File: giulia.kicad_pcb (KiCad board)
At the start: 2 copper layers, 240.9 x 112.5 mm, 129 parts, among them J1 AVR-ISP-6, J2 0548190519, SW1 RESET, SW2 BOOT, U1 ATmega32A-PU, Y1 16 MHz

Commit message: rev1 of routing done
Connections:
- U1 pad 18: Net-(U1-Pad18) -> RGB
- U1 pad 20: RGB -> Net-(U1-Pad20)
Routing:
- net +5V: track 139.9 -> 772.8 mm, vias 1 -> 3
- net GND: track 155.9 -> 781.5 mm
- net SDA: track 0.00 -> 100.2 mm, vias 0 -> 1
- net SCL: track 0.00 -> 96.6 mm, vias 0 -> 1
- net Net-(D50-Pad4): track 0.00 -> 83.5 mm, vias 0 -> 1
- net Net-(D51-Pad2): track 0.00 -> 66.6 mm, vias 0 -> 2
- net Net-(D52-Pad2): track 0.00 -> 65.0 mm
- net Net-(D56-Pad2): track 0.00 -> 48.7 mm
- net Net-(D50-Pad2): track 0.00 -> 46.5 mm
- net Net-(D53-Pad2): track 0.00 -> 42.1 mm
- net Net-(D63-Pad2): track 0.00 -> 35.9 mm
- net Net-(D59-Pad2): track 0.00 -> 33.1 mm
- net Net-(D60-Pad2): track 0.00 -> 33.0 mm
- net Net-(D57-Pad2): track 0.00 -> 32.0 mm
- net Net-(D62-Pad2): track 0.00 -> 32.0 mm
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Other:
- board text added: "BOOT"
- board text added: "RESET"

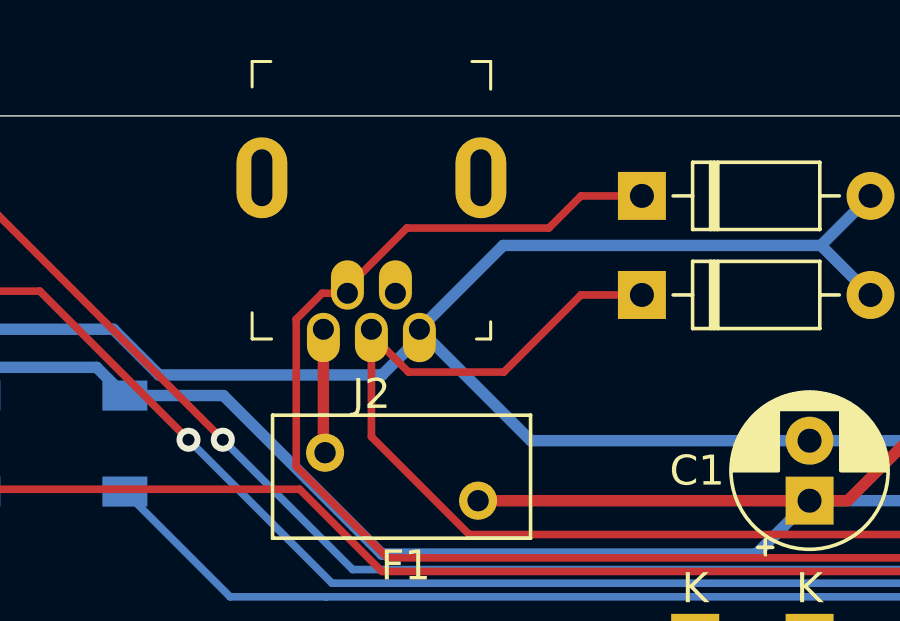
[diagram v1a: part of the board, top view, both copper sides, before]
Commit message: moved USB footprint to own lib
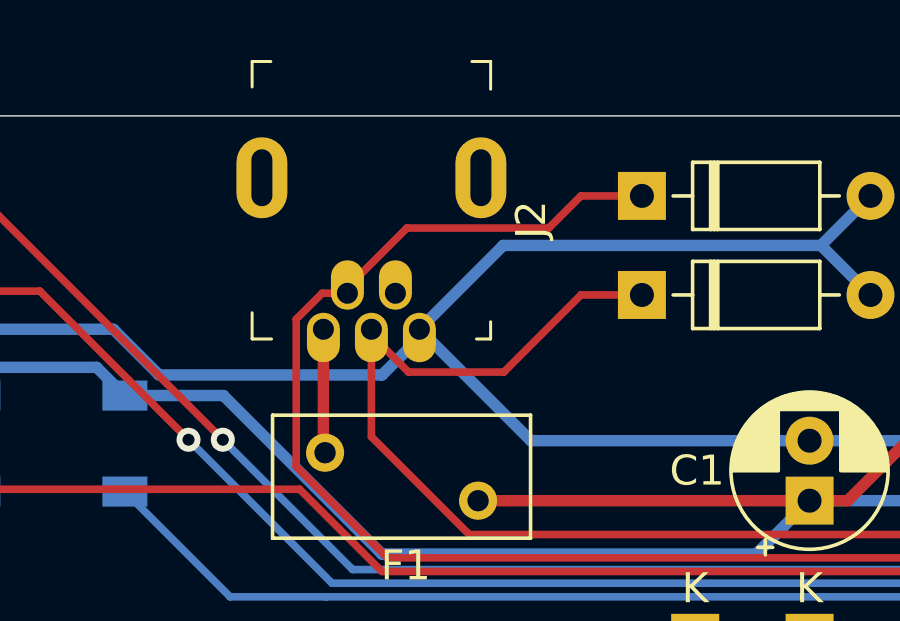
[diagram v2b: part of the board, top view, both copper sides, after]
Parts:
- J2: footprint digikey-footprints:USB_Mini_B_Female_548190519 -> giulia:USB_Mini_B_Female_548190519
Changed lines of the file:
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@@
     (add_net VCC)
   )
+  (module giulia:USB_Mini_B_Female_548190519 (layer F.Cu)
+    (at 94.615 27.686 270)
+    (fp_text reference J2 (at -3.65 -5.325 90) (layer F.SilkS)
+      (effects (font (size 1 1) (thickness 0.15)))
+    )
+    (fp_text value 0548190519 (at -4.2 6.35 90) (layer F.Fab)
+      (effects (font (size 1 1) (thickness 0.15)))
+    )
+    (fp_text user %R (at -5.7 -0.075 90) (layer F.Fab)
+      (effects (font (size 1 1) (thickness 0.15)))
+    )
+    (fp_line (start 1.35 -4.75) (end 1.35 4.75) (layer F.CrtYd) (width 0.05))
+    (fp_line (start -9.05 -4.75) (end -9.05 4.75) (layer F.CrtYd) (width 0.05))
+    (fp_line (start -9.05 4.75) (end 1.35 4.75) (layer F.CrtYd) (width 0.05))
+    (fp_line (start -9.05 -4.75) (end 1.35 -4.75) (layer F.CrtYd) (width 0.05))
+    (fp_line (start 0.325 3.975) (end 0.3 3.975) (layer F.SilkS) (width 0.1))
+    (fp_line (start 0.325 3.325) (end 0.325 3.975) (layer F.SilkS) (width 0.1))
+    (fp_line (start -0.55 3.975) (end 0.3 3.975) (layer F.SilkS) (width 0.1))
+    (fp_line (start -8.075 3.975) (end -8.925 3.975) (layer F.SilkS) (width 0.1))
+    (fp_line (start -8.925 3.975) (end -8.925 3.35) (layer F.SilkS) (width 0.1))
+    (fp_line (start -8 -3.975) (end -8.925 -3.975) (layer F.SilkS) (width 0.1))
+    (fp_line (start -8.925 -3.975) (end -8.925 -3.35) (layer F.SilkS) (width 0.1))
+    (fp_line (start -0.25 -3.975) (end 0.325 -3.975) (layer F.SilkS) (width 0.1))
+    (fp_line (start 0.325 -3.975) (end 0.325 -3.5) (layer F.SilkS) (width 0.1))
+    (fp_line (start -8.8 3.85) (end 0.2 3.85) (layer F.Fab) (width 0.1))
+    (fp_line (start -8.8 -3.85) (end 0.2 -3.85) (layer F.Fab) (width 0.1))
+    (fp_line (start 0.2 -3.85) (end 0.2 3.85) (layer F.Fab) (width 0.1))
+    (fp_line (start -8.8 -3.85) (end -8.8 3.85) (layer F.Fab) (width 0.1))
+    (pad SH thru_hole oval (at -5.05 3.65 270) (size 2.7 1.7) (drill oval 1.9 0.7) (layers *.Cu *.Mask)
+      (net 80 "Net-(J2-PadSH)"))
+    (pad SH thru_hole oval (at -5.05 -3.65 270) (size 2.7 1.7) (drill oval 1.9 0.7) (layers *.Cu *.Mask)
+      (net 80 "Net-(J2-PadSH)"))
+    (pad 4 thru_hole oval (at -1.2 0.8 270) (size 1.65 1.1) (drill 0.7 (offset -0.275 0)) (layers *.Cu *.Mask)
+      (net 57 "Net-(D49-Pad1)"))
+    (pad 2 thru_hole oval (at -1.2 -0.8 270) (size 1.65 1.1) (drill 0.7 (offset -0.275 0)) (layers *.Cu *.Mask)
+      (net 81 "Net-(J2-Pad2)"))
+    (pad 5 thru_hole oval (at 0 1.6 270) (size 1.65 1.1) (drill 0.7 (offset 0.275 0)) (layers *.Cu *.Mask)
+      (net 75 VCC))
+    (pad 1 thru_hole oval (at 0 -1.6 270) (size 1.65 1.1) (drill 0.7 (offset 0.275 0)) (layers *.Cu *.Mask)
+      (net 1 GND))
+    (pad 3 thru_hole oval (at 0 0 270) (size 1.65 1.1) (drill 0.7 (offset 0.275 0)) (layers *.Cu *.Mask)
+      (net 56 "Net-(D48-Pad1)"))
+  )
   (module Capacitor_THT:C_Disc_D5.0mm_W2.5mm_P5.00mm (layer F.Cu)
     (at 150.241 53.594)
@@
     )
   )
-  (module digikey-footprints:USB_Mini_B_Female_548190519 (layer F.Cu)
-    (at 94.615 27.686 270)
-    (fp_text reference J2 (at 2.159 0 180) (layer F.SilkS)
-      (effects (font (size 1 1) (thickness 0.15)))
-    )
-    (fp_text value 0548190519 (at -9.906 0 180) (layer F.Fab)
-      (effects (font (size 1 1) (thickness 0.15)))
-    )
-    (fp_line (start -8.8 -3.85) (end -8.8 3.85) (layer F.Fab) (width 0.1))
-    (fp_line (start 0.2 -3.85) (end 0.2 3.85) (layer F.Fab) (width 0.1))
-    (fp_line (start -8.8 -3.85) (end 0.2 -3.85) (layer F.Fab) (width 0.1))
-    (fp_line (start -8.8 3.85) (end 0.2 3.85) (layer F.Fab) (width 0.1))
-    (fp_line (start 0.325 -3.975) (end 0.325 -3.5) (layer F.SilkS) (width 0.1))
-    (fp_line (start -0.25 -3.975) (end 0.325 -3.975) (layer F.SilkS) (width 0.1))
-    (fp_line (start -8.925 -3.975) (end -8.925 -3.35) (layer F.SilkS) (width 0.1))
-    (fp_line (start -8 -3.975) (end -8.925 -3.975) (layer F.SilkS) (width 0.1))
-    (fp_line (start -8.925 3.975) (end -8.925 3.35) (layer F.SilkS) (width 0.1))
-    (fp_line (start -8.075 3.975) (end -8.925 3.975) (layer F.SilkS) (width 0.1))
-    (fp_line (start -0.55 3.975) (end 0.3 3.975) (layer F.SilkS) (width 0.1))
-    (fp_line (start 0.325 3.325) (end 0.325 3.975) (layer F.SilkS) (width 0.1))
-    (fp_line (start 0.325 3.975) (end 0.3 3.975) (layer F.SilkS) (width 0.1))
-    (fp_line (start -9.05 -4.75) (end 1.35 -4.75) (layer F.CrtYd) (width 0.05))
-    (fp_line (start -9.05 4.75) (end 1.35 4.75) (layer F.CrtYd) (width 0.05))
-    (fp_line (start -9.05 -4.75) (end -9.05 4.75) (layer F.CrtYd) (width 0.05))
-    (fp_line (start 1.35 -4.75) (end 1.35 4.75) (layer F.CrtYd) (width 0.05))
-    (fp_text user %R (at -5.7 -0.075 90) (layer F.Fab)
-      (effects (font (size 1 1) (thickness 0.15)))
-    )
-    (pad SH thru_hole oval (at -5.05 3.65 270) (size 2.7 1.7) (drill oval 1.9 0.7) (layers *.Cu *.Mask)
-      (net 80 "Net-(J2-PadSH)"))
-    (pad SH thru_hole oval (at -5.05 -3.65 270) (size 2.7 1.7) (drill oval 1.9 0.7) (layers *.Cu *.Mask)
-      (net 80 "Net-(J2-PadSH)"))
-    (pad 4 thru_hole oval (at -1.2 0.8 270) (size 1.65 1.1) (drill 0.7 (offset -0.275 0)) (layers *.Cu *.Mask)
-      (net 57 "Net-(D49-Pad1)"))
-    (pad 2 thru_hole oval (at -1.2 -0.8 270) (size 1.65 1.1) (drill 0.7 (offset -0.275 0)) (layers *.Cu *.Mask)
-      (net 81 "Net-(J2-Pad2)"))
-    (pad 5 thru_hole oval (at 0 1.6 270) (size 1.65 1.1) (drill 0.7 (offset 0.275 0)) (layers *.Cu *.Mask)
-      (net 75 VCC))
-    (pad 1 thru_hole oval (at 0 -1.6 270) (size 1.65 1.1) (drill 0.7 (offset 0.275 0)) (layers *.Cu *.Mask)
-      (net 1 GND))
-    (pad 3 thru_hole oval (at 0 0 270) (size 1.65 1.1) (drill 0.7 (offset 0.275 0)) (layers *.Cu *.Mask)
-      (net 56 "Net-(D48-Pad1)"))
-  )
   (module Fuse:Fuse_BelFuse_0ZRE0005FF_L8.3mm_W3.8mm (layer F.Cu)

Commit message: some PCB finishing touches
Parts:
- added G1: LOGO, giulia:Cuore_Sportivo, F.Cu at (229.9, 28.4)
- added M2,5: MountingHole_2.7mm_M2.5_ISO7380_Pad, MountingHole:MountingHole_2.7mm_M2.5_ISO7380_Pad, F.Cu at (69.8, 74.0)
- added M2,5: MountingHole_2.7mm_M2.5_ISO7380_Pad, MountingHole:MountingHole_2.7mm_M2.5_ISO7380_Pad, F.Cu at (222.2, 74.0)
- added M2,5: MountingHole_2.7mm_M2.5_ISO7380_Pad, MountingHole:MountingHole_2.7mm_M2.5_ISO7380_Pad, F.Cu at (150.7, 92.8)
- added M2,5: MountingHole_2.7mm_M2.5_ISO7380_Pad, MountingHole:MountingHole_2.7mm_M2.5_ISO7380_Pad, F.Cu at (231.8, 112.8)
- added M2,5: MountingHole_2.7mm_M2.5_ISO7380_Pad, MountingHole:MountingHole_2.7mm_M2.5_ISO7380_Pad, F.Cu at (59.7, 109.2)
- added M2,5: MountingHole_2.7mm_M2.5_ISO7380_Pad, MountingHole:MountingHole_2.7mm_M2.5_ISO7380_Pad, F.Cu at (267.5, 24.4)
- added M2,5: MountingHole_2.7mm_M2.5_ISO7380_Pad, MountingHole:MountingHole_2.7mm_M2.5_ISO7380_Pad, F.Cu at (34.2, 24.4)
- D48, D49: footprint Diode_THT:D_DO-35_SOD27_P7.62mm_Horizontal -> giulia:D_DO-35_SOD27_P7.62mm_Zener
- moved C3 22.7 mm to (155.3, 31.5), turned to 180 degrees
- moved C2 22.7 mm to (150.3, 53.6), turned to 0 degrees
- moved D48 1.52 mm to (105.2, 26.5)
- moved D49 1.52 mm to (105.2, 23.2)
- moved D52 0.64 mm to (152.8, 39.4)
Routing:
- net GND: track 781.5 -> 784.2 mm
- net ROW0: track 246.3 -> 244.4 mm
- net Net-(D49-Pad1): track 51.6 -> 53.1 mm
- net Net-(D48-Pad1): track 46.3 -> 47.8 mm
- net +5V: track 772.8 -> 771.7 mm
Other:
- board size 240.9 x 112.5 mm -> 242.2 x 113.8 mm
- board text added: "SCL"
- board text added: "SDA"
- board text added: "VCC"
- board text removed: "5V"

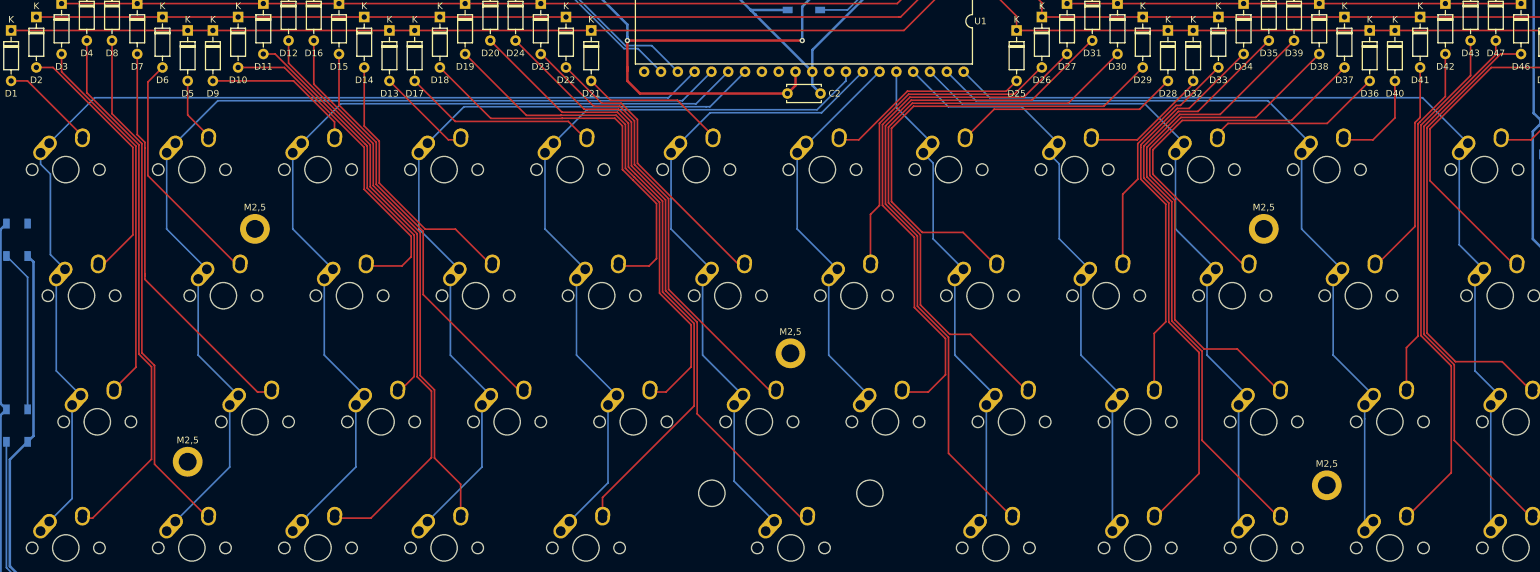
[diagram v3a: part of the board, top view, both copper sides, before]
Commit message: redid column traces
to be further away from pin support holes (just to be sure)
also made the PCB a tiny bit larger for underglow trace safety
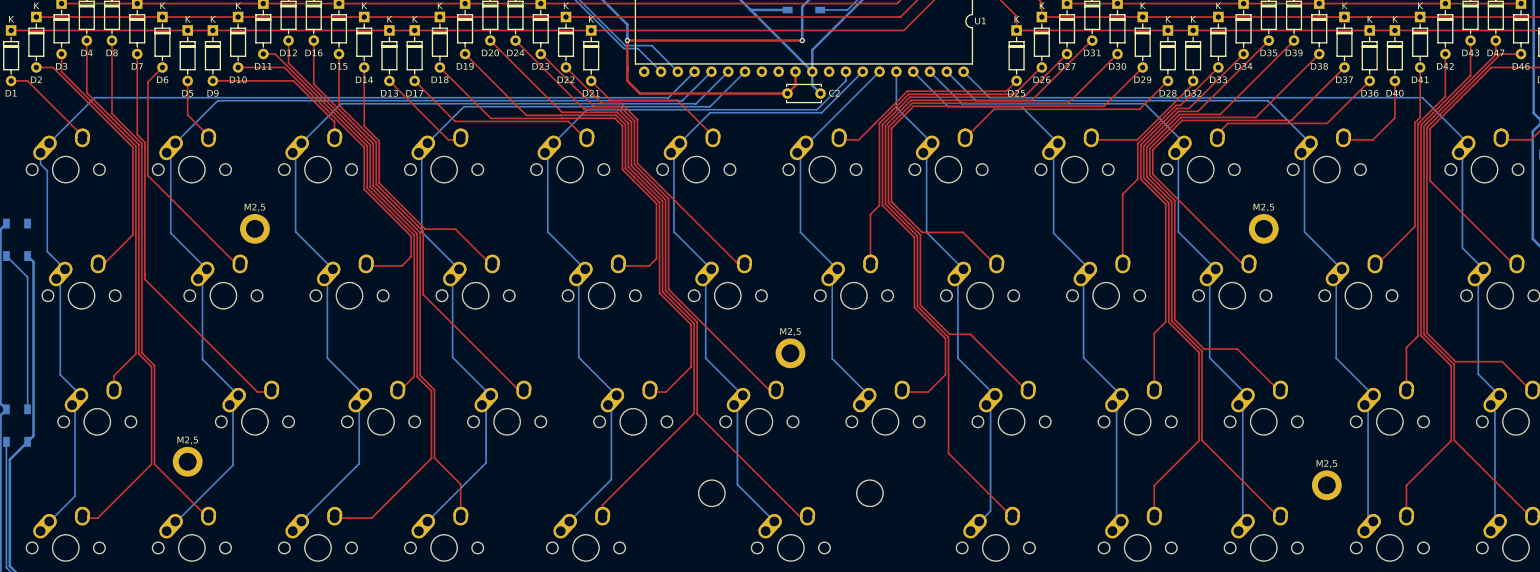
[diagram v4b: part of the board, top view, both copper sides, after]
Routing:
- net COL0: track 159.2 -> 161.8 mm
- net COL1: track 146.7 -> 149.1 mm
- net COL9: track 102.1 -> 101.2 mm
- net COL11: track 137.9 -> 137.1 mm
- net COL8: track 85.6 -> 84.9 mm
- net COL7: track 73.3 -> 73.9 mm
- net COL3: track 113.6 -> 114.2 mm

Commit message: rearranged RGB
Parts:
- added G2: LOGO, giulia:Biscione, F.Cu at (70.1, 91.9)
- moved D51 133.9 mm to (217.8, 31.5)
- moved D50 114.8 mm to (152.8, 39.4), turned to 180 degrees
- moved D52 111.0 mm to (263.5, 31.5)
- moved D64 72.4 mm to (38.2, 31.5), turned to 180 degrees
- moved D59 71.8 mm to (114.9, 128.9)
- moved D55 70.2 mm to (250.8, 128.9), turned to 0 degrees
- moved D65 66.8 mm to (83.9, 31.5), turned to 180 degrees
- moved D58 64.5 mm to (150.7, 128.9)
- moved D60 64.4 mm to (86.4, 128.9)
- moved D61 64.1 mm to (50.8, 128.9)
- moved D57 64.1 mm to (186.7, 128.9)
- moved D56 63.6 mm to (215.3, 128.9), turned to 0 degrees
- moved D54 61.1 mm to (267.3, 92.5), turned to 90 degrees
- moved D62 58.2 mm to (33.9, 103.8), turned to 270 degrees
- moved D53 56.1 mm to (265.9, 60.3), turned to 90 degrees
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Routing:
- net Net-(D50-Pad4): track 83.5 -> 35.7 mm
- net Net-(D52-Pad2): track 64.7 -> 25.4 mm
- net Net-(D51-Pad2): track 66.9 -> 42.1 mm, vias 2 -> 0
- net Net-(D56-Pad2): track 48.7 -> 25.0 mm
- net Net-(D54-Pad2): track 25.4 -> 48.7 mm
- net +5V: track 771.7 -> 794.3 mm, vias 3 -> 2
- net Net-(D50-Pad2): track 46.5 -> 64.7 mm
- net Net-(D64-Pad2): track 24.5 -> 42.1 mm
- net GND: track 784.2 -> 769.9 mm
- net Net-(D53-Pad2): track 42.1 -> 29.6 mm
- net Net-(D63-Pad2): track 35.9 -> 46.9 mm
- net Net-(D61-Pad2): track 25.0 -> 35.9 mm
- net Net-(D59-Pad2): track 33.1 -> 25.0 mm
- net Net-(D58-Pad2): track 25.0 -> 33.0 mm
- net Net-(D62-Pad2): track 32.0 -> 24.5 mm
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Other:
- board text added: "Giulia, rev. 1, TuCZnak, 2021"

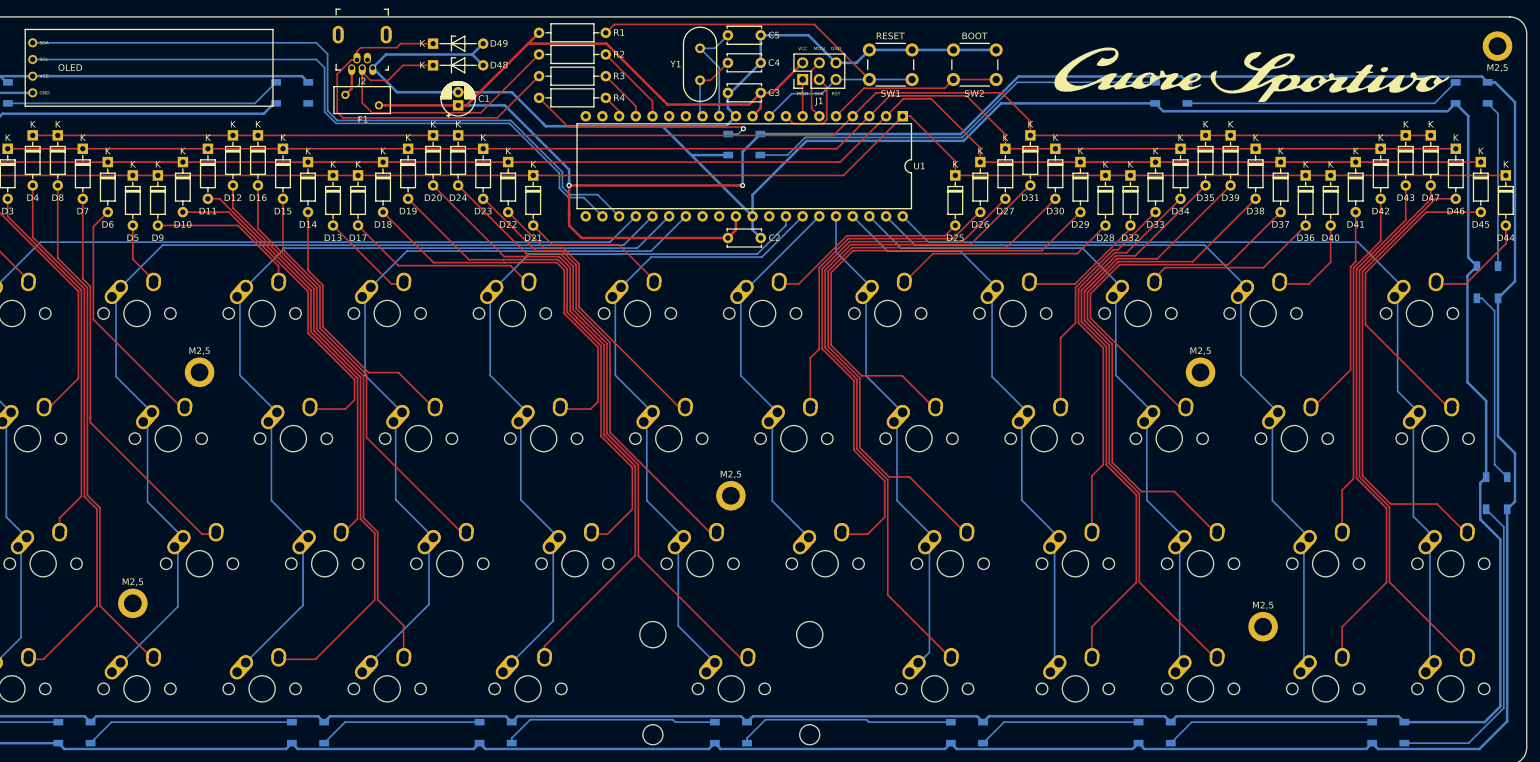
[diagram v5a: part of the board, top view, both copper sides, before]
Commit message: minor trace adjustments
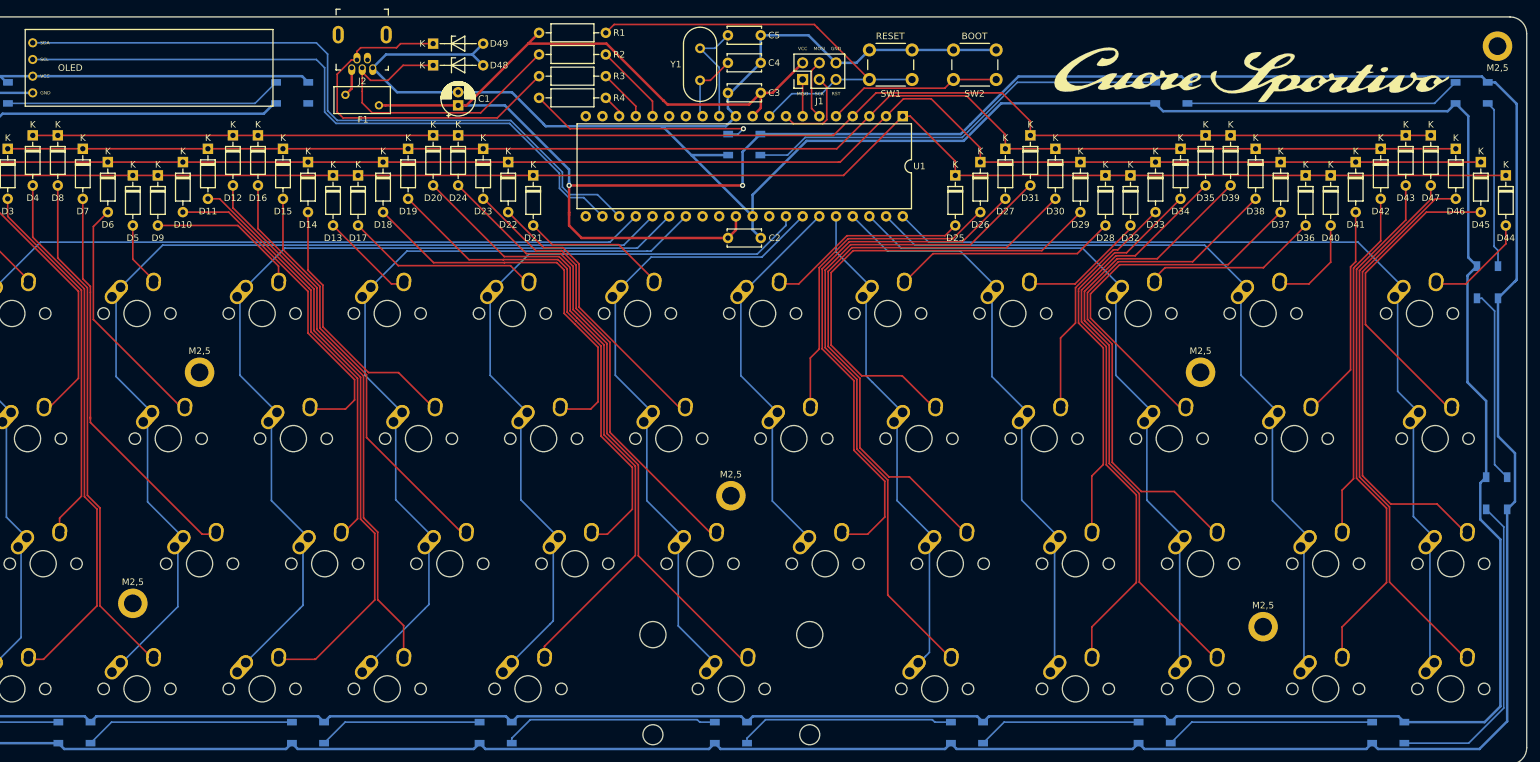
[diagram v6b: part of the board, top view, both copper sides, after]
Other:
- board text removed: "SCL"
- board text removed: "SDA"
